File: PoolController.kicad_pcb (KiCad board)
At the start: 2 copper layers, 80 x 75 mm, 22 parts, among them J1 RJ12, J2 RJ12, J3 Header, J4 Conn_02x12_Counter_Clockwise, Q1 MMBT3904, U1 LM2678S-5.0/NOPB

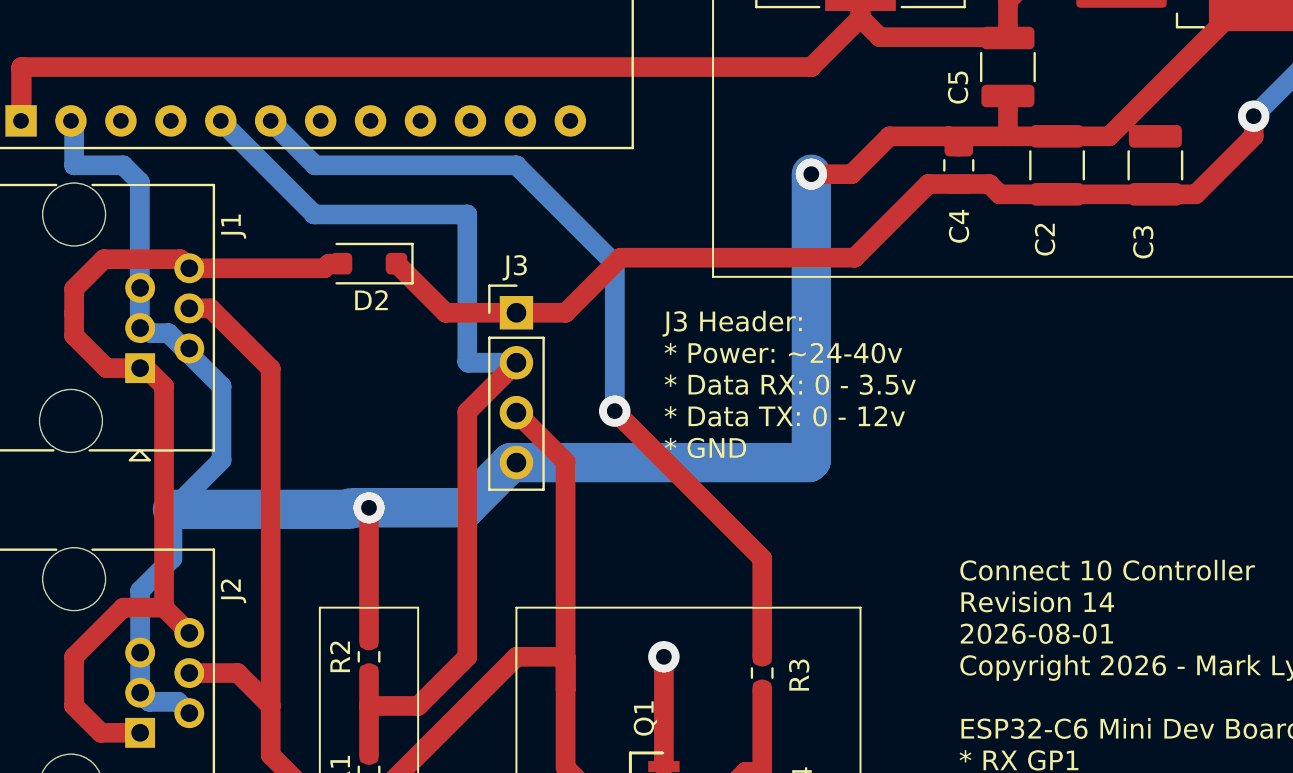
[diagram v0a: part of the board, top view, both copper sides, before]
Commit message: Add revision 15 RX clamp and TX drive prototype package
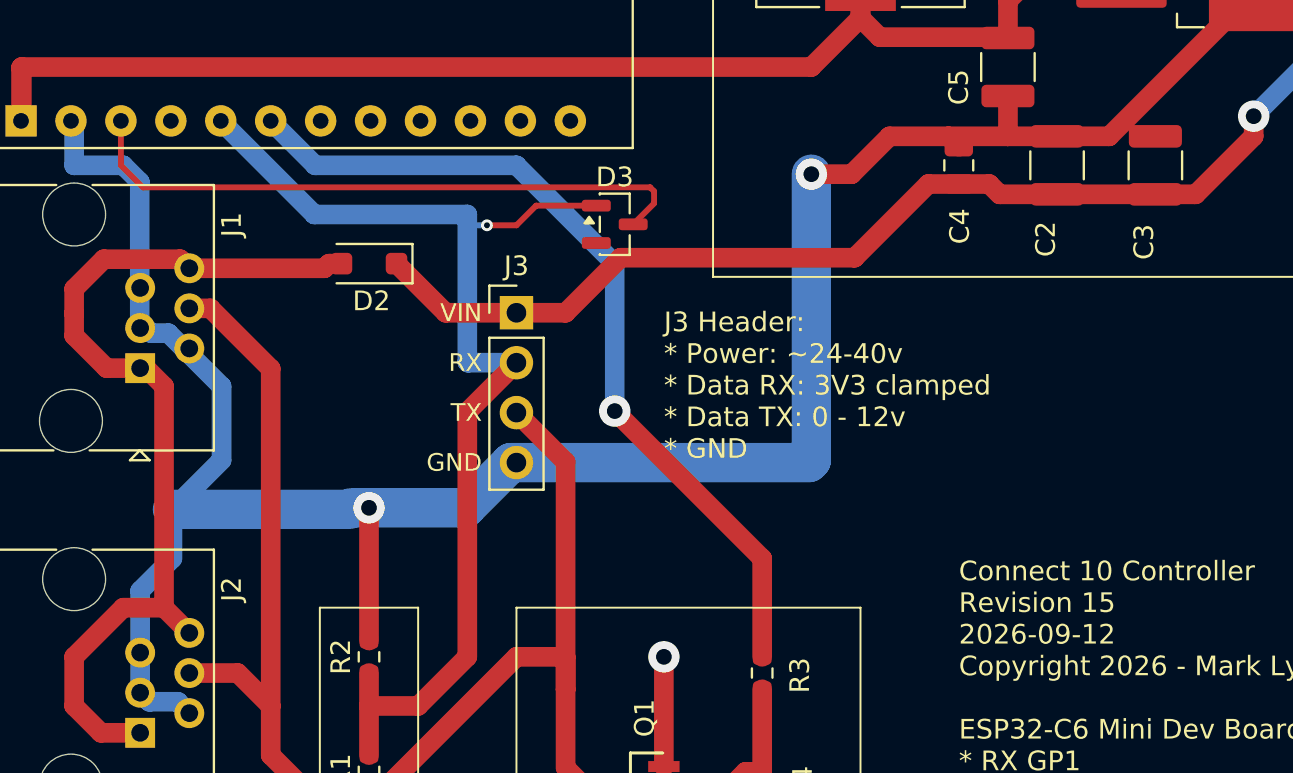
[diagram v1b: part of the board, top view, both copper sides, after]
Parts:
- added D3: BAT54, Package_TO_SOT_SMD:SOT-23, F.Cu at (100.0, 73.0)
- J1, J2: footprint Connector_RJ:RJ25_RJ12_5324_mini -> PoolController:RJ12_5324_6P6C
- R3: value R1k -> R560
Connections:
- net Net-(J3-Pin_2) renamed /RX
- J4 pad 3: unconnected-(J4-Pin_3-Pad3) -> /+3V3_MODULE
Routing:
- net /+3V3_MODULE: track 0.00 -> 32.0 mm
- net /RX: track 50.7 -> 57.7 mm, vias 0 -> 1
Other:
- board text added: "GND"
- board text added: "J3 Header: * Power: ~24-40v * Data RX: 3V3 clamped * Data TX: 0 - 12v * GND"
- board text added: "RX"
- board text added: "TX"
- board text added: "VIN"
- board text removed: "J3 Header: * Power: ~24-40v * Data RX: 0 - 3.5v * Data TX: 0 - 12v * GND"

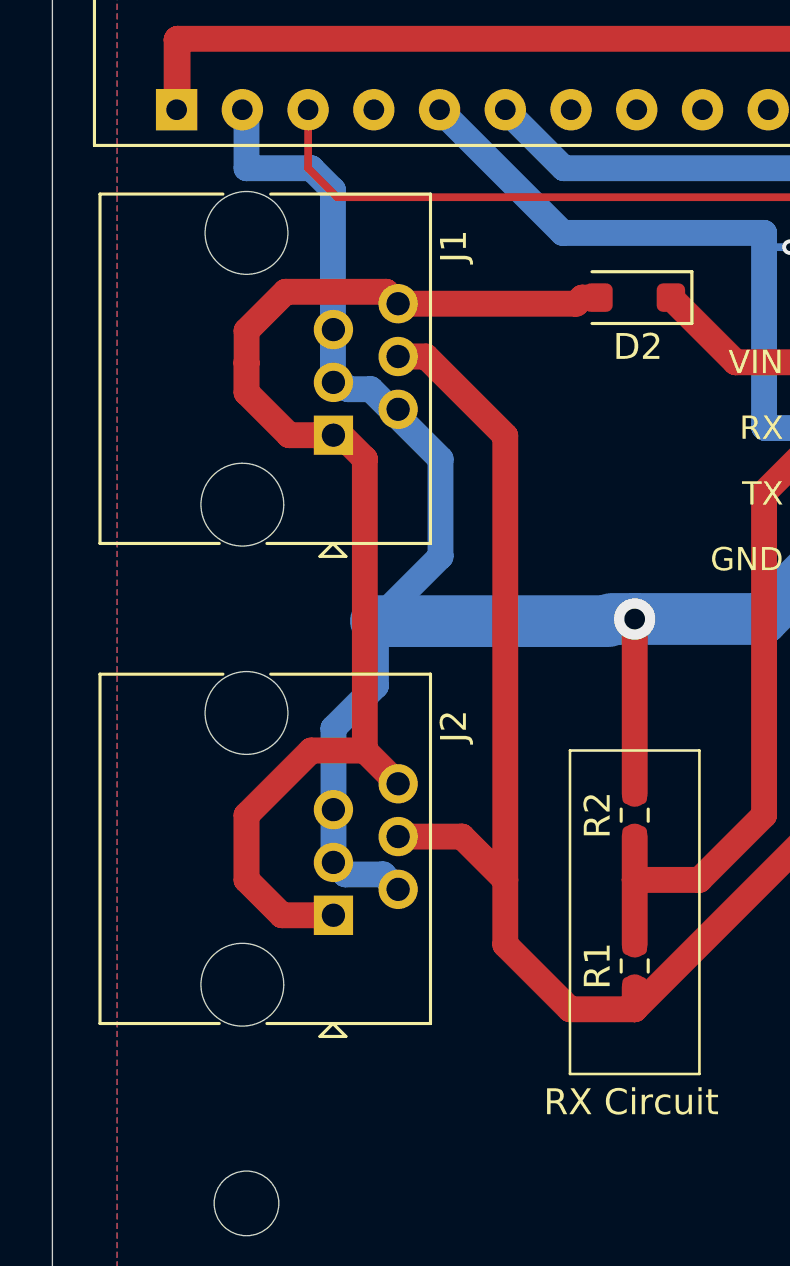
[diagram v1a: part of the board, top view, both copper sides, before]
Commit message: Specify stocked RJ12 sockets and prepare PCBWay carrier assembly package
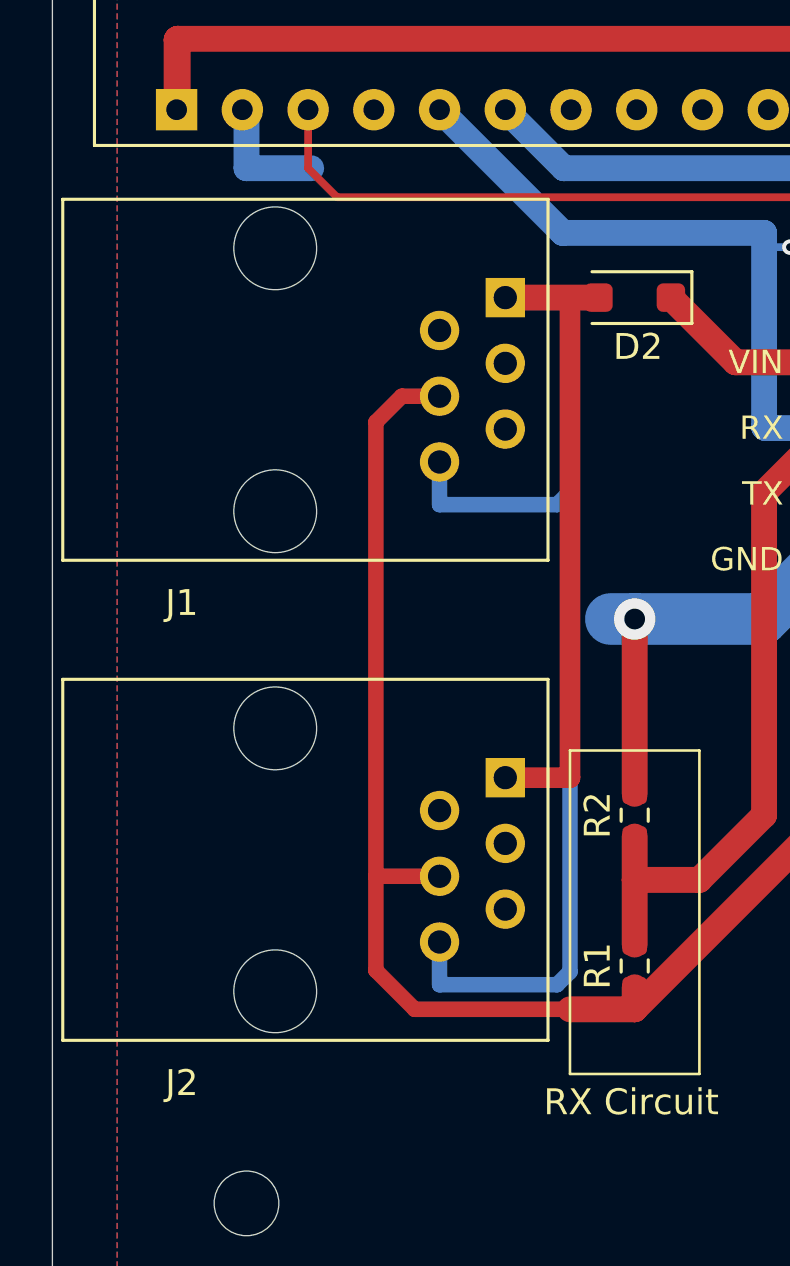
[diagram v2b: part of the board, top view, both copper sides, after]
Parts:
- J1, J2: footprint PoolController:RJ12_5324_6P6C -> PoolController:RJ12_Ckmtw_R-RJ11R06P-A000
- moved J1 7.19 mm to (82.5, 75.0)
- moved J2 7.19 mm to (82.5, 93.5)
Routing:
- net GND (from connector): track 164.2 -> 121.1 mm
- net +24V (from connector): track 47.7 -> 58.4 mm
- net Net-(J3-Pin_3): track 74.3 -> 75.5 mm

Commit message: Replace legacy carrier parts and preserve enclosure mounting fit
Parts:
- added J5: SSW-109-01-T-S, PoolController:Samtec_SSW-109-01-T-S_1x09, F.Cu at (69.8, 52.5)
- J4: value Conn_02x12_Counter_Clockwise -> SSW-109-01-T-S; footprint Package_DIP:DIP-24_18.0mmx34.29mm_W15.24mm_Socket -> PoolController:Samtec_SSW-109-01-T-S_1x09
- turned J4 to 0 degrees
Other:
- board text added: "5V END"
- board text removed: "<- Align pins to end"
